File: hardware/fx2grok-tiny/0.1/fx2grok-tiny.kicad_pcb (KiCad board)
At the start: 2 copper layers, 13 x 13 mm, 28 parts, among them IC1 CY7C68013A-56, P1 CONN_5, P2 CONN_5, U1 MICRO-USB-B-SMD, U2 MIC5319, X1 QUARTZCMS4

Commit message: layout: Re-read netlist.
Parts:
- removed X1: QUARTZCMS4, ABM11
- added Y1: Crystal, ABM11, F.Cu at (74.2, 60.8)
- P1, P2: value CONN_5 -> CONN_01X05
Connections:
- C1 pad 1: +3.3V -> +3V3
- C10 pad 1: +3.3V -> +3V3
- C11 pad 1: +3.3V -> +3V3
- C12 pad 1: +3.3V -> +3V3
- C13 pad 1: +3.3V -> +3V3
- C16 pad 1: +3.3V -> +3V3
- C2 pad 1: +3.3V -> +3V3
- C3 pad 1: +3.3V -> +3V3
- C5 pad 1: +3.3V -> +3V3
- C6 pad 1: +3.3V -> +3V3
- C7 pad 1: +3.3V -> +3V3
- C8 pad 1: +3.3V -> +3V3
- D1 pad 1: N-000044 -> Net-(D1-Pad1)
- IC1 pad 11: +3.3V -> +3V3
- IC1 pad 17: +3.3V -> +3V3
- IC1 pad 27: +3.3V -> +3V3
- IC1 pad 3: +3.3V -> +3V3
- IC1 pad 32: +3.3V -> +3V3
- IC1 pad 43: +3.3V -> +3V3
- IC1 pad 55: +3.3V -> +3V3
- IC1 pad 7: +3.3V -> +3V3
- R1 pad 1: +3.3V -> +3V3
- R2 pad 1: +3.3V -> +3V3
- R3 pad 1: /SDA -> /SCL
- R3 pad 2: +3.3V -> +3V3
- R4 pad 1: N-000044 -> /SDA
- R4 pad 2: /PA0 -> +3V3
- R5 pad 1: /SCL -> Net-(D1-Pad1)
- R5 pad 2: +3.3V -> /PA0
- U2 pad 5: +3.3V -> +3V3
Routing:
- net +3.3V: track 42.8 -> 0.00 mm, vias 3 -> 0
- net +3V3: track 0.00 -> 39.1 mm, vias 0 -> 3
- net /SDA: track 3.30 -> 0.08 mm
- net /PA0: track 2.13 -> 0.45 mm, vias 1 -> 0
- net Net-(D1-Pad1): track 0.00 -> 0.70 mm
- net N-000044: track 0.70 -> 0.00 mm

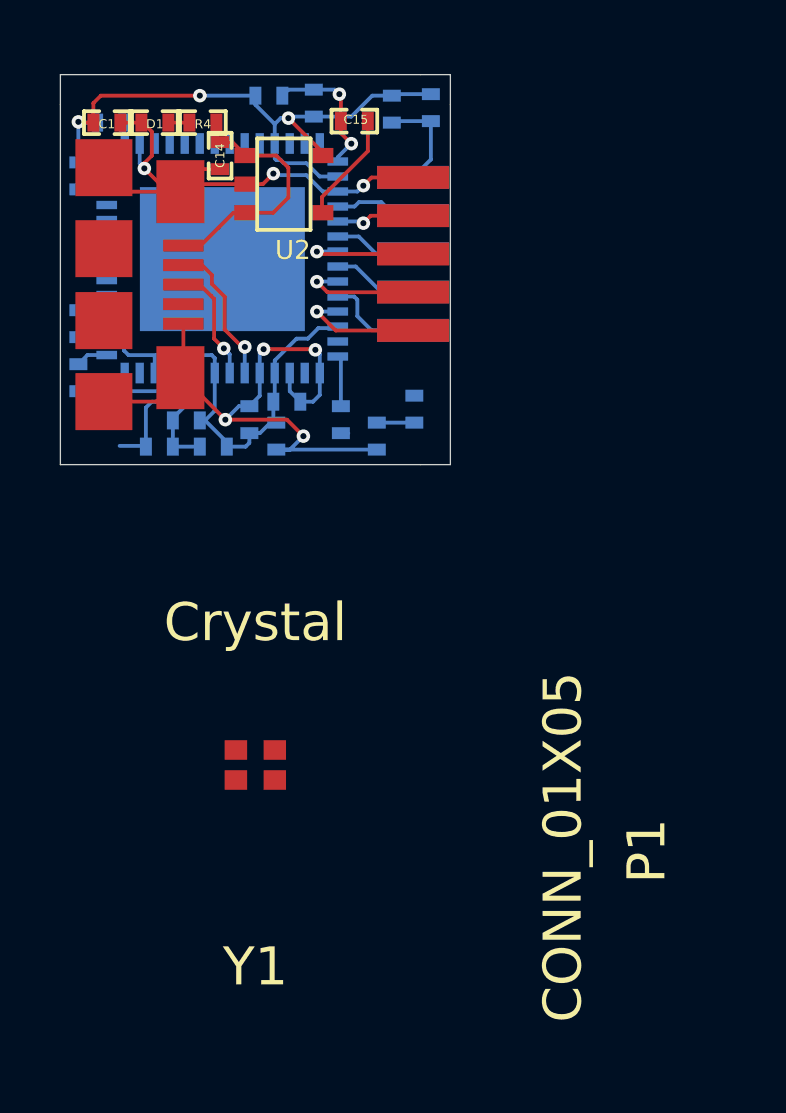
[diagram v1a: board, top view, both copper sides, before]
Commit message: Replace crystal symbol with a 4-pin SMD crystal variant.
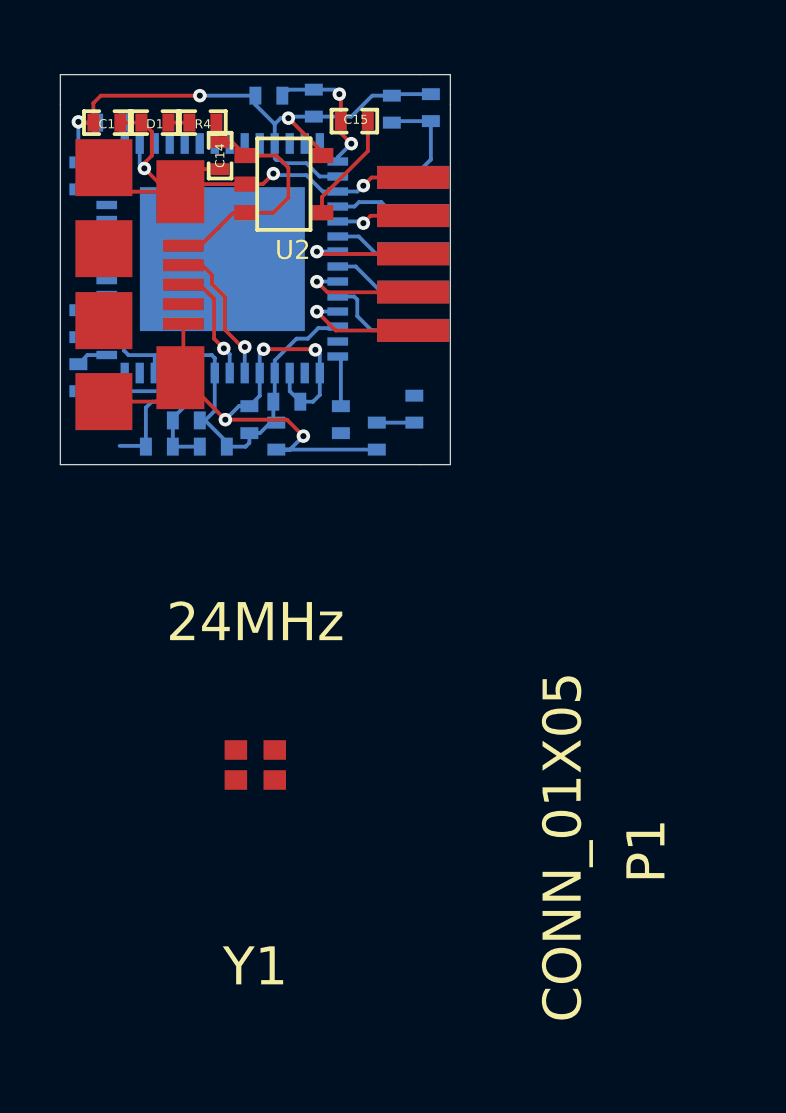
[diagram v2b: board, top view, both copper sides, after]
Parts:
- Y1: value Crystal -> 24MHz
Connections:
- Y1 pad 2: /XTALOUT -> GND
- Y1 pad 3: (no net) -> /XTALOUT
- Y1 pad 4: (no net) -> GND
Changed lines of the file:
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@@
 (kicad_pcb (version 4) (host pcbnew 4.0.5+dfsg1-4)
   (general
-    (links 81)
-    (no_connects 15)
+    (links 83)
+    (no_connects 17)
     (area 67.688459 37.736779 80.713581 50.761901)
     (thickness 1.6002)
@@
       (effects (font (thickness 0.3048)))
     )
-    (fp_text value Crystal (at 0 -4.7498) (layer F.SilkS)
+    (fp_text value 24MHz (at 0 -4.7498) (layer F.SilkS)
       (effects (font (thickness 0.3048)))
     )
@@
       (net 17 /XTALIN) (clearance 0.09906))
     (pad 2 smd rect (at 0.6477 0.50038) (size 0.7493 0.65024) (layers Front F.Paste F.Mask)
+      (net 19 GND) (clearance 0.09906))
+    (pad 3 smd rect (at 0.6477 -0.50038) (size 0.7493 0.65024) (layers Front F.Paste F.Mask)
       (net 18 /XTALOUT) (clearance 0.09906))
-    (pad 3 smd rect (at 0.6477 -0.50038) (size 0.7493 0.65024) (layers Front F.Paste F.Mask)
-      (clearance 0.09906))
     (pad 4 smd rect (at -0.65024 -0.50038) (size 0.7493 0.65024) (layers Front F.Paste F.Mask)
-      (clearance 0.09906))
+      (net 19 GND) (clearance 0.09906))
   )
   (gr_line (start 79.70012 50.7492) (end 80.70088 50.7492) (angle 90) (layer Edge.Cuts) (width 0.0254))

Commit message: Finish initial layout, fixup various details.
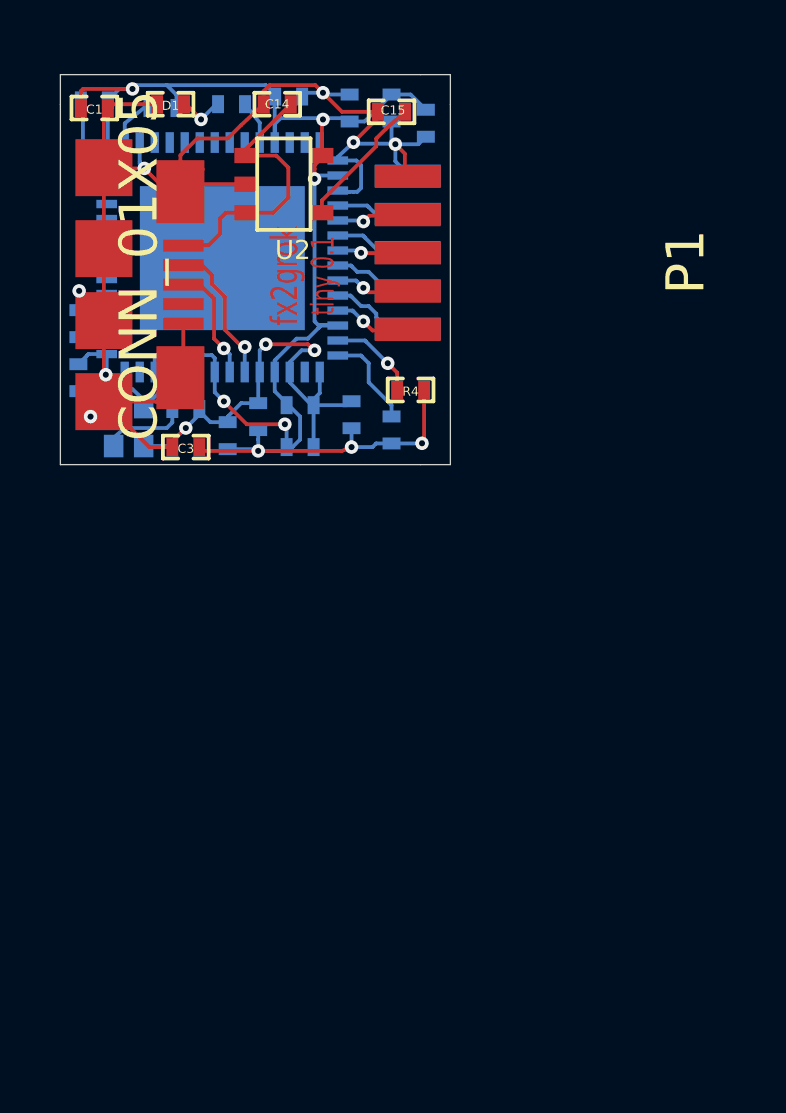
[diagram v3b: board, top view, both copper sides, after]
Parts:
- C3: moved to F.Cu
- P1, P2: footprint CONN-5x1-SMD-127MM -> fx2grok-tiny:CONN-5x1-SMD-127MM
- U1: footprint MICRO-USB-B-SMD -> fx2grok-tiny:MICRO-USB-B-SMD
- Y1: moved to B.Cu
- moved Y1 12.0 mm to (70.0, 49.5), turned to 90 degrees
- moved R4 11.3 mm to (79.4, 48.3)
- moved R5 11.1 mm to (73.4, 38.7), turned to 0 degrees
- moved C6 2.61 mm to (77.4, 49.1), turned to 90 degrees
- moved C7 2.58 mm to (75.7, 50.2), turned to 0 degrees
- moved R1 2.57 mm to (68.8, 38.6), turned to 180 degrees
- moved C14 2.56 mm to (74.9, 38.7), turned to 180 degrees
- moved R2 1.81 mm to (71.1, 38.9), turned to 180 degrees
- moved C4 1.53 mm to (71.9, 48.9)
- moved C15 1.28 mm to (78.7, 39.0)
- moved C5 1.20 mm to (77.3, 38.9)
- moved R3 1.03 mm to (78.7, 49.6)
- moved C3 0.89 mm to (71.9, 50.2)
- moved D1 0.81 mm to (71.4, 38.7)
- moved C13 0.66 mm to (75.3, 38.5)
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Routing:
- net GND: track 54.0 -> 77.5 mm, vias 9 -> 10
- net +3V3: track 39.1 -> 57.8 mm, vias 3 -> 8
- net /SDA: track 0.08 -> 3.19 mm, vias 0 -> 1
- net /WAKEUP: track 1.14 -> 3.18 mm
- net /PB7: track 2.76 -> 4.49 mm
- net +5V: track 7.79 -> 9.48 mm
- net /PB4: track 3.94 -> 2.37 mm
- net /SCL: track 1.70 -> 3.23 mm
- net /PB2: track 4.05 -> 2.67 mm
- net /PB0: track 4.17 -> 2.79 mm
- net /PA0: track 0.45 -> 1.45 mm
- net /RESET#: track 0.71 -> 1.64 mm
- net Net-(C15-Pad1): track 3.69 -> 4.53 mm
- net Net-(D1-Pad1): track 0.70 -> 1.44 mm, vias 0 -> 1
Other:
- board text added: "fx2grok"
- board text added: "tiny 0.1"
